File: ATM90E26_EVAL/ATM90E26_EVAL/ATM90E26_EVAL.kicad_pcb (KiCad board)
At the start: 2 copper layers, 80 x 70 mm, 43 parts, among them J1 AC INPUT, J2 Current Input, J3 12V Supply, J4 3.3V Supply, J5 Conn_01x10, U1 HLK-10M12, U2 ATM90E26-YU, U3 MIC5209-3.3YS-TR, U4 24C02Cx-x-SN, Y1 8.192Mhz

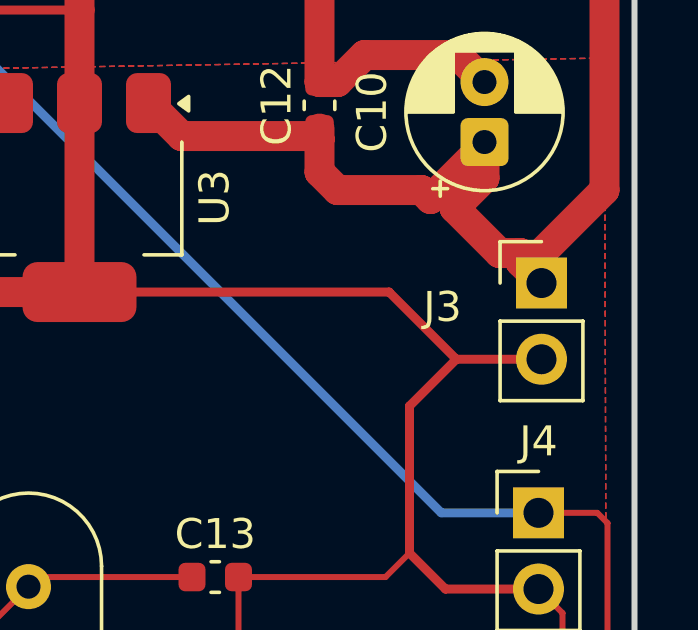
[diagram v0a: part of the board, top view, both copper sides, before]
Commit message: Optimize PCB design rules and ground plane
- Assign LINE/NEUT nets to HighVoltage net class (1.0mm clearance)
- Change zone fill from hatched to solid for better EMI shielding
- Reduce zone clearance from 0.5mm to 0.35mm for denser copper fill
- Enable corner smoothing and island removal for manufacturability
- Add silkscreen labels for pin identification on back layer
- Set output directory for gerber files

Co-Authored-By: Claude Opus 4.5 <noreply@anthropic.com>
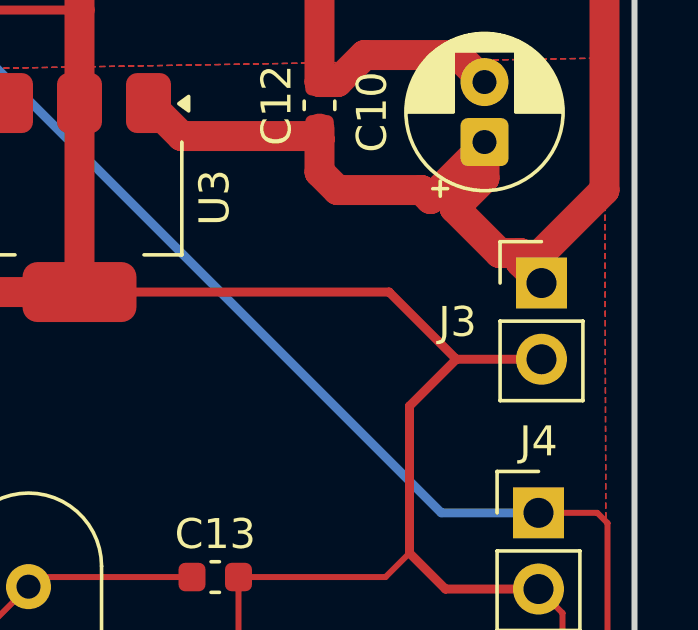
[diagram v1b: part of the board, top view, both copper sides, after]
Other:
- board text added: "12V"
- board text added: "3.3V"
- board text added: "CF1"
- board text added: "CLK"
- board text added: "CS"
- board text added: "GND"
- board text added: "IRQ"
- board text added: "L"
- board text added: "N"
- board text added: "SCL"
- board text added: "SDA"
- board text added: "SDI"
- board text added: "SDO"
- board text added: "VIVI"
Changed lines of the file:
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@@
 			(outputformat 1)
 			(mirror no)
-			(drillshape 1)
+			(drillshape 0)
 			(scaleselection 1)
-			(outputdirectory "")
+			(outputdirectory "../output/")
 		)
 	)
@@
 		(tags "Through hole pin header THT 1x02 2.54mm single row")
 		(property "Reference" "J3"
-			(at -3.3 0.8 0)
+			(at -2.8 1.3 0)
 			(layer "F.SilkS")
 			(effects
@@
 		(layer "Edge.Cuts")
 	)
+	(gr_text "CS"
+		(at 151.7 115.2 0)
+		(layer "B.SilkS")
+		(effects
+			(font
+				(size 0.75 0.75)
+				(thickness 0.0625)
+			)
+			(justify left bottom mirror)
+		)
+	)
+	(gr_text "3.3V"
+		(at 139.1 115.2 0)
+		(layer "B.SilkS")
+		(effects
+			(font
+				(size 0.75 0.75)
+				(thickness 0.09375)
+			)
+			(justify left bottom mirror)
+		)
+	)
+	(gr_text "GND"
+		(at 142 115.2 0)
+		(layer "B.SilkS")
+		(effects
+			(font
+				(size 0.75 0.75)
+				(thickness 0.09375)
+			)
+			(justify left bottom mirror)
+		)
+	)
+	(gr_text "SDI"
+		(at 144.4 115.2 0)
+		(layer "B.SilkS")
+		(effects
+			(font
+				(size 0.75 0.75)
+				(thickness 0.09375)
+			)
+			(justify left bottom mirror)
+		)
+	)
+	(gr_text "SDO"
+		(at 147 115.2 0)
+		(layer "B.SilkS")
+		(effects
+			(font
+				(size 0.75 0.75)
+				(thickness 0.09375)
+			)
+			(justify left bottom mirror)
+		)
+	)
+	(gr_text "CLK"
+		(at 149.5 115.2 0)
+		(layer "B.SilkS")
+		(effects
+			(font
+				(size 0.75 0.75)
+				(thickness 0.09375)
+			)
+			(justify left bottom mirror)
+		)
+	)
+	(gr_text "IRQ"
+		(at 154.5 115.1 0)
+		(layer "B.SilkS")
+		(effects
+			(font
+				(size 0.75 0.75)
+				(thickness 0.09375)
+			)
+			(justify left bottom mirror)
+		)
+	)
+	(gr_text "CF1"
+		(at 157.1 115.1 0)
+		(layer "B.SilkS")
+		(effects
+			(font
+				(size 0.75 0.75)
+				(thickness 0.09375)
+			)
+			(justify left bottom mirror)
+		)
+	)
+	(gr_text "SCL"
+		(at 159.6 115.1 0)
+		(layer "B.SilkS")
+		(effects
+			(font
+				(size 0.75 0.75)
+				(thickness 0.09375)
+			)
+			(justify left bottom mirror)
+		)
+	)
+	(gr_text "SDA"
+		(at 162.6 115.1 0)
+		(layer "B.SilkS")
+		(effects
+			(font
+				(size 0.75 0.75)
+				(thickness 0.09375)
+			)
+			(justify left bottom mirror)
+		)
+	)
+	(gr_text "L"
+		(at 103.9 54.4 0)
+		(layer "B.SilkS")
+		(effects
+			(font
+				(size 1.5 1.5)
+				(thickness 0.3)
+				(bold yes)
+			)
+			(justify left bottom mirror)
+		)
+	)
+	(gr_text "N"
+		(at 104 59.3 0)
+		(layer "B.SilkS")
+		(effects
+			(font
+				(size 1.5 1.5)
+				(thickness 0.3)
+				(bold yes)
+			)
+			(justify left bottom mirror)
+		)
+	)
+	(gr_text "VIVI"
+		(at 161.8 113 0)
+		(layer "B.SilkS")
+		(effects
+			(font
+				(size 1.5 1.5)
+				(thickness 0.3)
+				(bold yes)
+			)
+			(justify left bottom mirror)
+		)
+	)
+	(gr_text "3.3V"
+		(at 174.7 99.8 0)
+		(layer "B.SilkS")
+		(effects
+			(font
+				(size 1.5 1.5)
+				(thickness 0.3)
+				(bold yes)
+			)
+			(justify left bottom mirror)
+		)
+	)
+	(gr_text "12V"
+		(at 174.8 91.8 0)
+		(layer "B.SilkS")
+		(effects
+			(font
+				(size 1.5 1.5)
+				(thickness 0.3)
+				(bold yes)
+			)
+			(justify left bottom mirror)
+		)
+	)
+	(gr_text "GND"
+		(at 174.8 102.6 0)
+		(layer "B.SilkS")
+		(effects
+			(font
+				(size 1.5 1.5)
+				(thickness 0.3)
+				(bold yes)
+			)
+			(justify left bottom mirror)
+		)
+	)
+	(gr_text "GND"
+		(at 174.9 95.2 0)
+		(layer "B.SilkS")
+		(effects
+			(font
+				(size 1.5 1.5)
+				(thickness 0.3)
+				(bold yes)
+			)
+			(justify left bottom mirror)
+		)
+	)
 	(segment
 		(start 165.25 106.2)
@@
 		(priority 1)
 		(connect_pads
-			(clearance 0.5)
+			(clearance 0.35)
 		)
 		(min_thickness 0.25)
 		(fill yes
-			(mode hatch)
 			(thermal_gap 0.5)
 			(thermal_bridge_width 0.5)
 			(smoothing chamfer)
 			(island_removal_mode 0)
-			(hatch_thickness 1)
-			(hatch_gap 1.5)
-			(hatch_orientation 0)
-			(hatch_border_algorithm hatch_thickness)
-			(hatch_min_hole_area 0.15)
 		)
 		(polygon
@@
 		(hatch edge 0.5)
 		(connect_pads
-			(clearance 0.5)
+			(clearance 0.35)
 		)
 		(min_thickness 0.25)
 		(fill yes
-			(mode hatch)
 			(thermal_gap 0.5)
 			(thermal_bridge_width 0.5)
 			(smoothing chamfer)
 			(island_removal_mode 0)
-			(hatch_thickness 1)
-			(hatch_gap 1.5)
-			(hatch_orientation 0)
-			(hatch_border_algorithm hatch_thickness)
-			(hatch_min_hole_area 0.15)
 		)
 		(polygon
